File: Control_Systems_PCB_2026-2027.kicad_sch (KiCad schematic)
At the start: 27 parts, among them J1 USB_C_Receptacle_USB2.0_16P, J2 5-1814832-2, U1 STM32F446VETx, U2 LSM6DSOXTR, U3 MS5611-01BA, U4 USBLC6-2SC6, U5 NEO-M9N

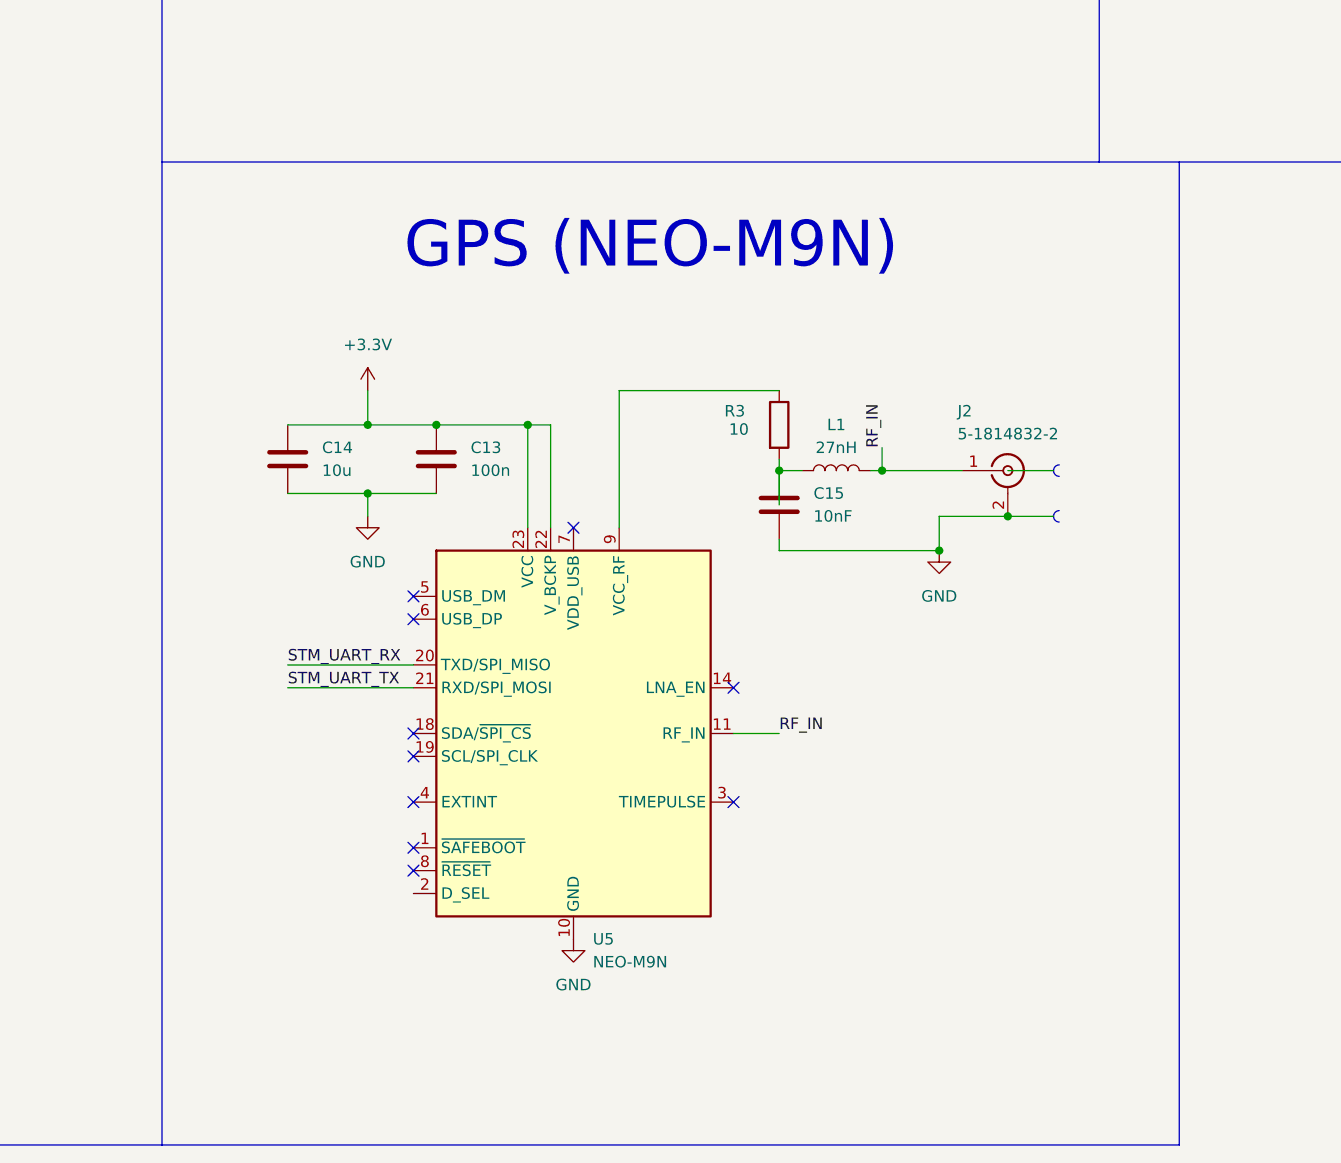
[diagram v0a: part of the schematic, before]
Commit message: Fix: put each schematic onto it's own page to prevent conflicts
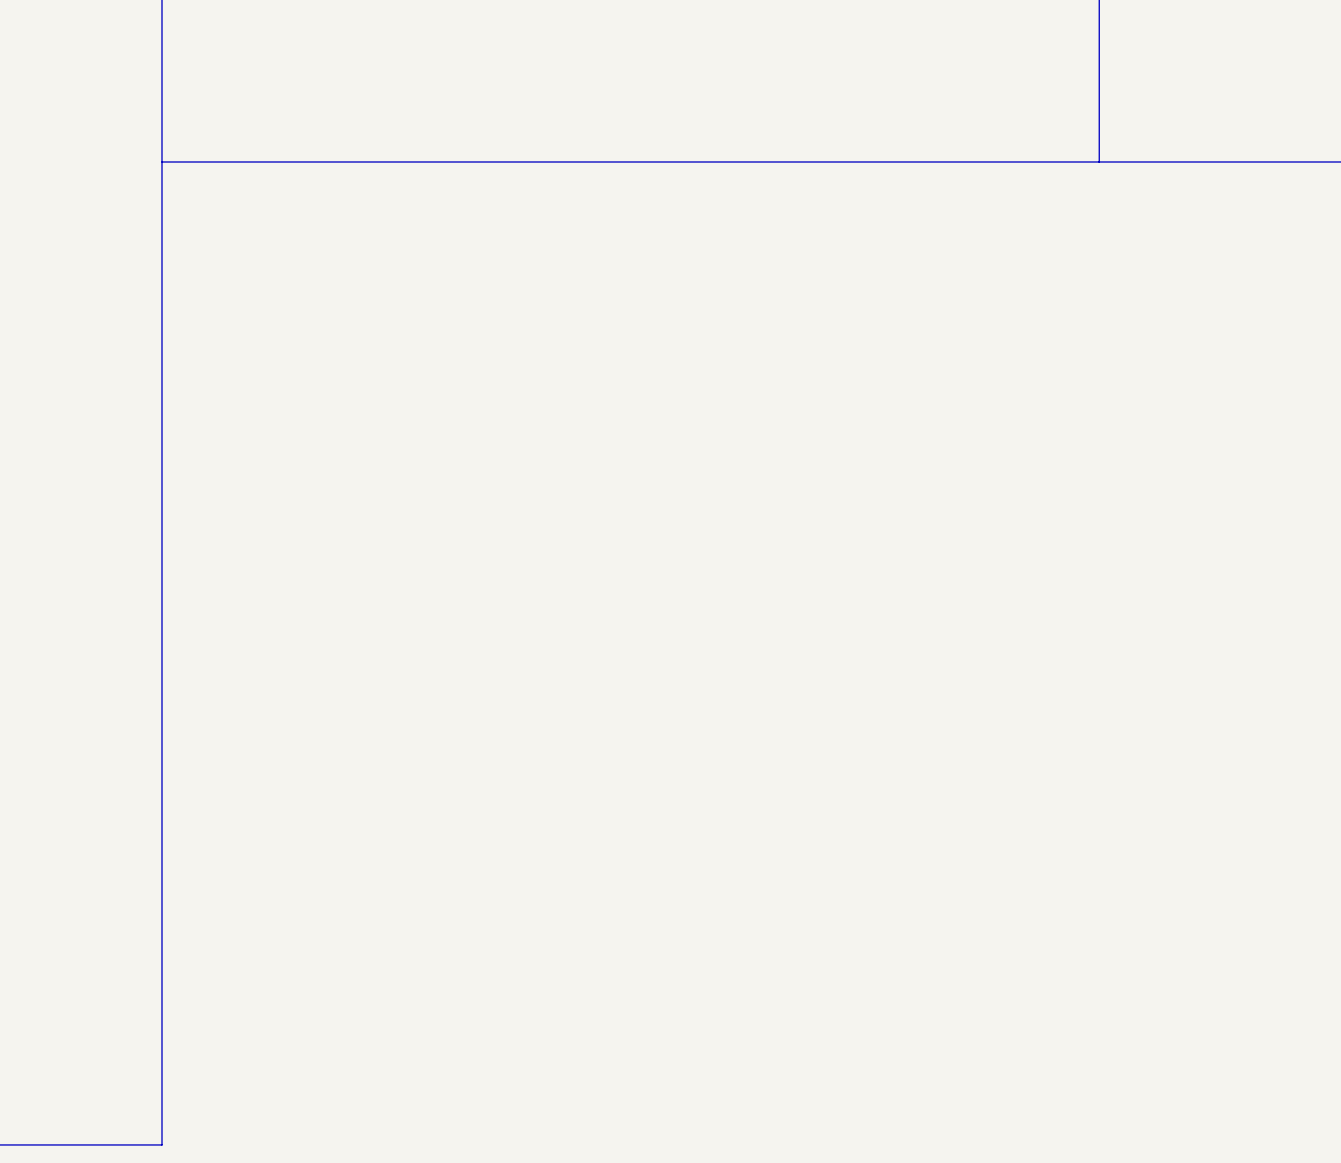
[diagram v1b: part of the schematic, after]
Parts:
- removed C13: 100n, symbol Device:C
- removed C14: 10u, symbol Device:C
- removed C15: 10nF, symbol Device:C
- removed J2: 5-1814832-2, symbol Connector:Conn_Coaxial
- removed L1: 27nH, Valve:Valve_Noval_P, symbol Device:L
- removed R3: 10, symbol Device:R
- removed U5: NEO-M9N, RF_GPS:ublox_NEO, symbol RF_GPS:NEO-M9N
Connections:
- no-connect marks 14 -> 4
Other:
- note removed: "GPS (NEO-M9N)"

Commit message: Fix: removed extra components on main sheet
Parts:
- removed C10, C11, C12: 100n, symbol Device:C
- removed J1: USB_C_Receptacle_USB2.0_16P, symbol Connector:USB_C_Receptacle_USB2.0_16P
- removed R1, R2: 5.1K, symbol Device:R
- removed U2: LSM6DSOXTR, LSM6DSOXTR:PQFN50P250X300X86-14N, symbol LSM6DSOXTR:LSM6DSOXTR
- removed U3: MS5611-01BA, Package_LGA:LGA-8_3x5mm_P1.25mm, symbol Sensor_Pressure:MS5611-01BA
- removed U4: USBLC6-2SC6, Package_TO_SOT_SMD:SOT-23-6, symbol Power_Protection:USBLC6-2SC6
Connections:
- no-connect marks 4 -> 0
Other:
- note removed: "Barometer (MS5611)"
- note removed: "LSM6DSOXTR"
- note removed: "USB_C_Recepticle"

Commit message: fahhh
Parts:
- removed C1, C2, C3, C4, C5, C7: 100n, symbol Device:C
- removed C6, C8, C9: 1u, symbol Device:C
- removed FB1: 120R, symbol Device:FerriteBead
- removed U1: STM32F446VETx, Package_QFP:LQFP-100_14x14mm_P0.5mm, symbol MCU_ST_STM32F4:STM32F446VETx
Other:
- note removed: "STM32F446VETx MCU"
